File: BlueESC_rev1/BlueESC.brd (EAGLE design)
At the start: 40.6 x 57.1 mm, 69 parts, among them J1 AVR_SPI_PRG_6PTH, Q4 SI7370, Q5 SI7370, Q6 SI7370, Q7 SI7370, Q8 SI7370, Q9 SI7370, U1 ATMEGA168, U2 V_REG_LDOSMD, Y1 RESONATORSMD

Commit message: Added diodes and capacitors near fets. Need to verify necessary package sizes.
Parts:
- added C10, C11, C12: 1.2uF, SparkFun-Capacitors:0805
- added D1, D2, D3: Schottky, SparkFun-DiscreteSemi:SOD-323
- Q1, Q2, Q3: value (none) -> BC817-40W
- R17, R23, R28: value 470 -> 2.2K
- R18, R24, R29: value 1K -> 4.7K
- moved R23 1.11 mm to (17.9, 31.8)
- moved R24 0.95 mm to (14.3, 31.8)
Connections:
- new net N$1: C10.1, D1.C, R17.2
- new net N$13: C11.1, D2.C, R23.2
- new net N$15: C12.1, D3.C, R28.2
- net PHASE_A: now also C10.2
- net PHASE_B: now also C11.2
- net PHASE_C: now also C12.2
- net VBAT: now also D1.A, D2.A, D3.A; no longer R17.2, R23.2, R28.2
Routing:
- net VBAT: track 64.3 -> 17.2 mm, vias 2 -> 0
- net N$5: track 3.11 -> 0.25 mm
- net N$6: track 5.17 -> 3.06 mm
- net PWM_BH: track 23.6 -> 24.5 mm

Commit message: Small changes.
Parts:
- Q6: value SI7370 -> SiR158DP
- R1, R2, R3: value 33K -> 3.3K
- R4, R5, R6: value 33K -> 18K
- R7, R8, R9: value 10K -> 3.3K
- moved C10 12.8 mm to (1.43, 23.3), turned to 270 degrees
- moved D1 9.84 mm to (1.43, 29.7), turned to 90 degrees
- moved D2 8.70 mm to (11.4, 26.5)
- moved D3 4.97 mm to (31.3, 29.1)
- moved C12 0.57 mm to (31.4, 32.2)
- moved C11 0.16 mm to (19.7, 31.8), turned to 270 degrees
- moved Q4 0.16 mm to (5.24, 21.6)
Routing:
- net N$1: track 0.00 -> 17.4 mm, vias 0 -> 2
- net VBAT: track 17.2 -> 34.3 mm
- net N$13: track 0.00 -> 13.3 mm
- net PHASE_B: track 25.8 -> 36.4 mm
- net PHASE_A: track 33.5 -> 37.6 mm
- net N$15: track 0.00 -> 3.94 mm
- net N$5: track 0.25 -> 3.40 mm
- net N$6: track 3.06 -> 5.63 mm
- net PHASE_C: track 29.3 -> 30.8 mm
- net CENTER: track 49.4 -> 48.1 mm

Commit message: Changed value of charge pump capacitors because there are more package sizes available for 1.0uF.
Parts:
- C10, C11, C12: value 1.2uF -> 1uF
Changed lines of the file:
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@@
 <attribute name="PROD_ID" value="DIO-09646" x="31.27375" y="29.05125" size="1.778" layer="27" rot="R270" display="off"/>
 </element>
-<element name="C10" library="SparkFun-Capacitors" package="0805" value="1.2uF" x="1.42875" y="23.33625" rot="R270"/>
-<element name="C11" library="SparkFun-Capacitors" package="0805" value="1.2uF" x="19.685" y="31.75" rot="R270"/>
-<element name="C12" library="SparkFun-Capacitors" package="0805" value="1.2uF" x="31.4325" y="32.22625" rot="R90"/>
+<element name="C10" library="SparkFun-Capacitors" package="0805" value="1uF" x="1.42875" y="23.33625" rot="R270"/>
+<element name="C11" library="SparkFun-Capacitors" package="0805" value="1uF" x="19.685" y="31.75" rot="R270"/>
+<element name="C12" library="SparkFun-Capacitors" package="0805" value="1uF" x="31.4325" y="32.22625" rot="R90"/>
 </elements>
 <signals>

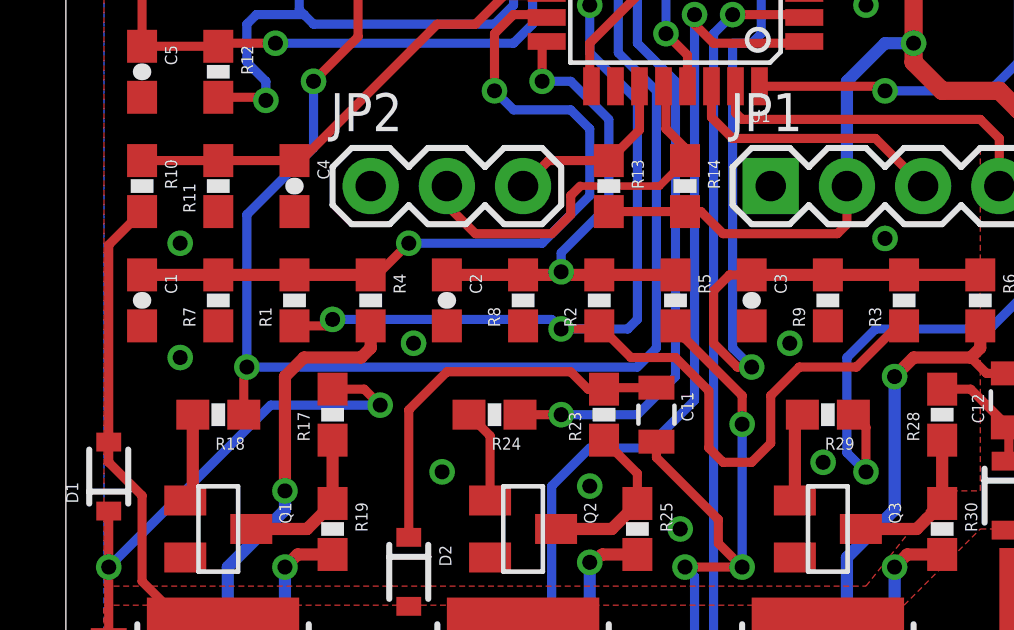
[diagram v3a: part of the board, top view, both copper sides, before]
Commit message: Removed sense filtering capacitors and changed voltage divider resistor values.
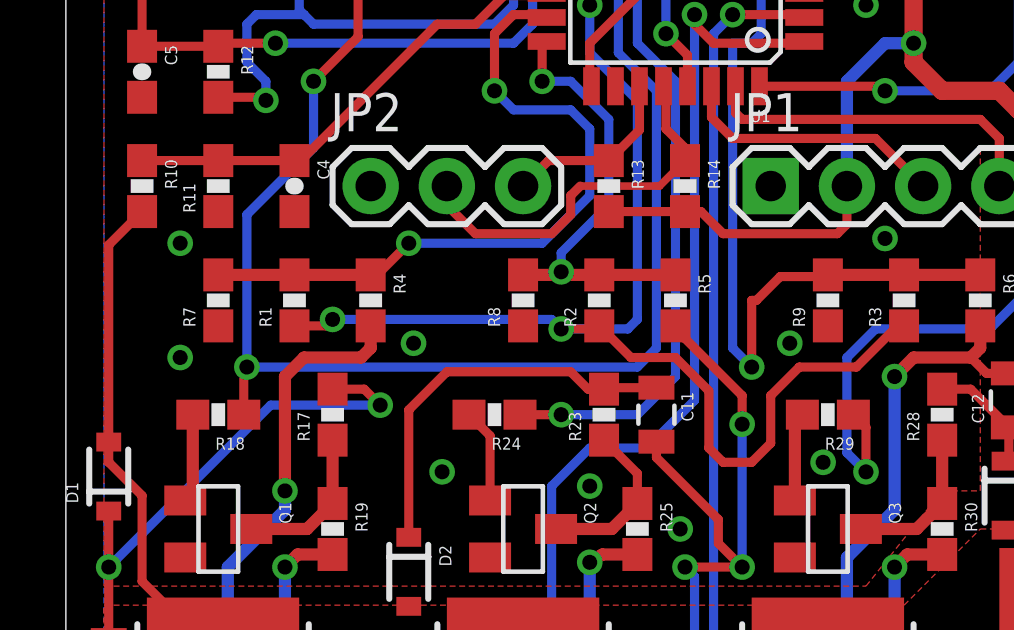
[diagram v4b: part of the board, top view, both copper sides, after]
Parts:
- removed C1, C2, C3: 0.01uF, SparkFun-Capacitors:0603-CAP
- R1, R2, R3: value 3.3K -> 47K
- R4, R5, R6: value 18K -> 47K
- R7, R8, R9: value 3.3K -> 4.7K
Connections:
- net GND: no longer C1.2, C2.2, C3.2
- net SENSE_A: no longer C1.1
- net SENSE_B: no longer C2.1
- net SENSE_C: no longer C3.1
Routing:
- net SENSE_B: track 18.8 -> 16.3 mm
- net SENSE_A: track 25.9 -> 23.3 mm
- net SENSE_C: track 34.2 -> 32.0 mm
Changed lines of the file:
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@@
 <elements>
 <element name="U1" library="SparkFun-DigitalIC" package="TQFP32-08" value="ATMEGA168" x="20.32" y="46.99" rot="R180"/>
-<element name="R1" library="SparkFun-Resistors" package="0603-RES" value="3.3K" x="7.62" y="35.56" rot="R90"/>
-<element name="R2" library="SparkFun-Resistors" package="0603-RES" value="3.3K" x="17.78" y="35.56" rot="R90"/>
-<element name="R3" library="SparkFun-Resistors" package="0603-RES" value="3.3K" x="27.94" y="35.56" rot="R90"/>
-<element name="R4" library="SparkFun-Resistors" package="0603-RES" value="18K" x="10.16" y="35.56" rot="R270"/>
-<element name="R5" library="SparkFun-Resistors" package="0603-RES" value="18K" x="20.32" y="35.56" rot="R270"/>
-<element name="R6" library="SparkFun-Resistors" package="0603-RES" value="18K" x="30.48" y="35.56" rot="R270"/>
-<element name="R7" library="SparkFun-Resistors" package="0603-RES" value="3.3K" x="5.08" y="35.56" rot="R90"/>
-<element name="R8" library="SparkFun-Resistors" package="0603-RES" value="3.3K" x="15.24" y="35.56" rot="R90"/>
-<element name="R9" library="SparkFun-Resistors" package="0603-RES" value="3.3K" x="25.4" y="35.56" rot="R90"/>
-<element name="C1" library="SparkFun-Capacitors" package="0603-CAP" value="0.01uF" x="2.54" y="35.56" rot="R270"/>
-<element name="C2" library="SparkFun-Capacitors" package="0603-CAP" value="0.01uF" x="12.7" y="35.56" rot="R270"/>
-<element name="C3" library="SparkFun-Capacitors" package="0603-CAP" value="0.01uF" x="22.86" y="35.56" rot="R270"/>
+<element name="R1" library="SparkFun-Resistors" package="0603-RES" value="47K" x="7.62" y="35.56" rot="R90"/>
+<element name="R2" library="SparkFun-Resistors" package="0603-RES" value="47K" x="17.78" y="35.56" rot="R90"/>
+<element name="R3" library="SparkFun-Resistors" package="0603-RES" value="47K" x="27.94" y="35.56" rot="R90"/>
+<element name="R4" library="SparkFun-Resistors" package="0603-RES" value="47K" x="10.16" y="35.56" rot="R270"/>
+<element name="R5" library="SparkFun-Resistors" package="0603-RES" value="47K" x="20.32" y="35.56" rot="R270"/>
+<element name="R6" library="SparkFun-Resistors" package="0603-RES" value="47K" x="30.48" y="35.56" rot="R270"/>
+<element name="R7" library="SparkFun-Resistors" package="0603-RES" value="4.7K" x="5.08" y="35.56" rot="R90"/>
+<element name="R8" library="SparkFun-Resistors" package="0603-RES" value="4.7K" x="15.24" y="35.56" rot="R90"/>
+<element name="R9" library="SparkFun-Resistors" package="0603-RES" value="4.7K" x="25.4" y="35.56" rot="R90"/>
 <element name="R10" library="SparkFun-Resistors" package="0603-RES" value="10K" x="2.54" y="39.37" rot="R270"/>
 <element name="R11" library="SparkFun-Resistors" package="0603-RES" value="1K" x="5.08" y="39.37" rot="R90"/>
@@
 <contactref element="R4" pad="1"/>
 <contactref element="R7" pad="2"/>
-<contactref element="C1" pad="1"/>
 <contactref element="U1" pad="23"/>
-<wire x1="2.54" y1="36.41" x2="5.08" y2="36.41" width="0.4064" layer="1"/>
 <wire x1="5.08" y1="36.41" x2="7.62" y2="36.41" width="0.4064" layer="1"/>
 <wire x1="7.62" y1="36.41" x2="10.16" y2="36.41" width="0.4064" layer="1"/>
@@
 <contactref element="R5" pad="1"/>
 <contactref element="R8" pad="2"/>
-<contactref element="C2" pad="1"/>
 <contactref element="U1" pad="24"/>
-<wire x1="12.7" y1="36.41" x2="15.24" y2="36.41" width="0.4064" layer="1"/>
 <wire x1="15.24" y1="36.41" x2="17.78" y2="36.41" width="0.4064" layer="1"/>
 <wire x1="17.78" y1="36.41" x2="20.32" y2="36.41" width="0.4064" layer="1"/>
@@
 <contactref element="R6" pad="1"/>
 <contactref element="R9" pad="2"/>
-<contactref element="C3" pad="1"/>
 <contactref element="U1" pad="25"/>
-<wire x1="22.86" y1="36.41" x2="25.4" y2="36.41" width="0.4064" layer="1"/>
 <wire x1="25.4" y1="36.41" x2="27.94" y2="36.41" width="0.4064" layer="1"/>
 <wire x1="27.94" y1="36.41" x2="30.48" y2="36.41" width="0.4064" layer="1"/>
-<wire x1="22.86" y1="36.41" x2="22.1225" y2="36.41" width="0.3048" layer="1"/>
-<wire x1="22.1225" y1="36.41" x2="21.59" y2="35.8775" width="0.3048" layer="1"/>
-<wire x1="21.59" y1="35.8775" x2="21.59" y2="34.13125" width="0.3048" layer="1"/>
 <via x="22.86" y="33.3375" extent="1-16" drill="0.5"/>
 <wire x1="22.86" y1="33.3375" x2="22.225" y2="33.9725" width="0.3048" layer="16"/>
@@
 <wire x1="23.1775" y1="44.45" x2="23.1775" y2="45.72" width="0.3048" layer="16"/>
 <wire x1="23.1775" y1="45.72" x2="22.5425" y2="46.355" width="0.3048" layer="16"/>
-<wire x1="21.59" y1="34.13125" x2="22.38375" y2="33.3375" width="0.3048" layer="1"/>
-<wire x1="22.38375" y1="33.3375" x2="22.86" y2="33.3375" width="0.3048" layer="1"/>
+<wire x1="22.86" y1="33.3375" x2="22.86" y2="35.56" width="0.3048" layer="1"/>
+<wire x1="22.86" y1="35.56" x2="23.01875" y2="35.56" width="0.3048" layer="1"/>
+<wire x1="23.01875" y1="35.56" x2="23.8125" y2="36.35375" width="0.3048" layer="1"/>
+<wire x1="23.8125" y1="36.35375" x2="25.34375" y2="36.35375" width="0.3048" layer="1"/>
+<wire x1="25.34375" y1="36.35375" x2="25.4" y2="36.41" width="0.3048" layer="1"/>
 </signal>
 <signal name="GND">
@@
 <contactref element="R9" pad="1"/>
 <contactref element="R8" pad="1"/>
-<contactref element="C1" pad="2"/>
-<contactref element="C3" pad="2"/>
-<contactref element="C2" pad="2"/>
 <contactref element="R11" pad="1"/>
 <contactref element="C4" pad="2"/>
